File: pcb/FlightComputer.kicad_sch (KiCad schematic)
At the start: 74 parts, among them J1 USB4105-GF-A, Q1 DMG3415U, Q2 Si2319CDS, Q3 Si2319CDS, SW1 RESET, SW2 BOOT, U2 ICM-42670-P, U3 ESP32-C3-MINI-1, U5 SY8088, U6 MCP73831T-2ACI/OT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

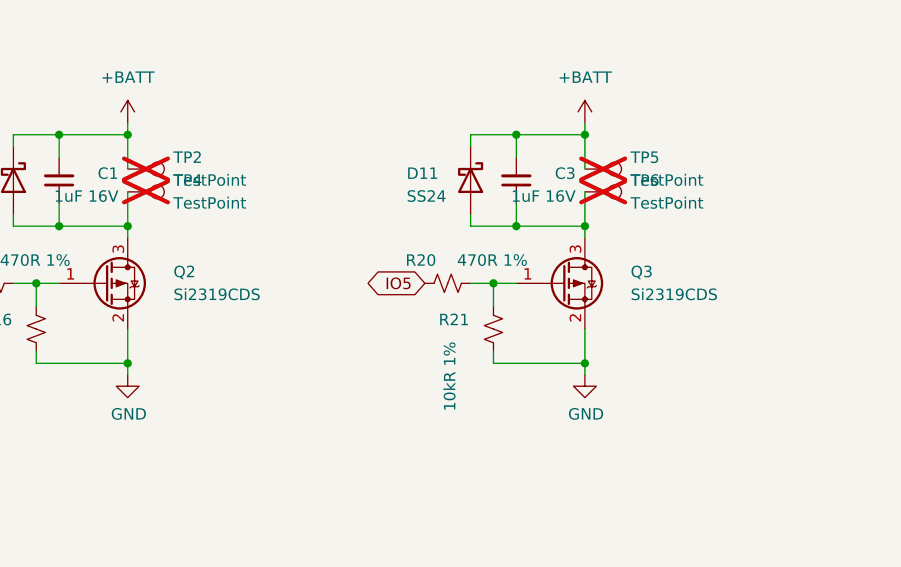
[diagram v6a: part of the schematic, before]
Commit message: change Si2319CDS to Si2302CDS
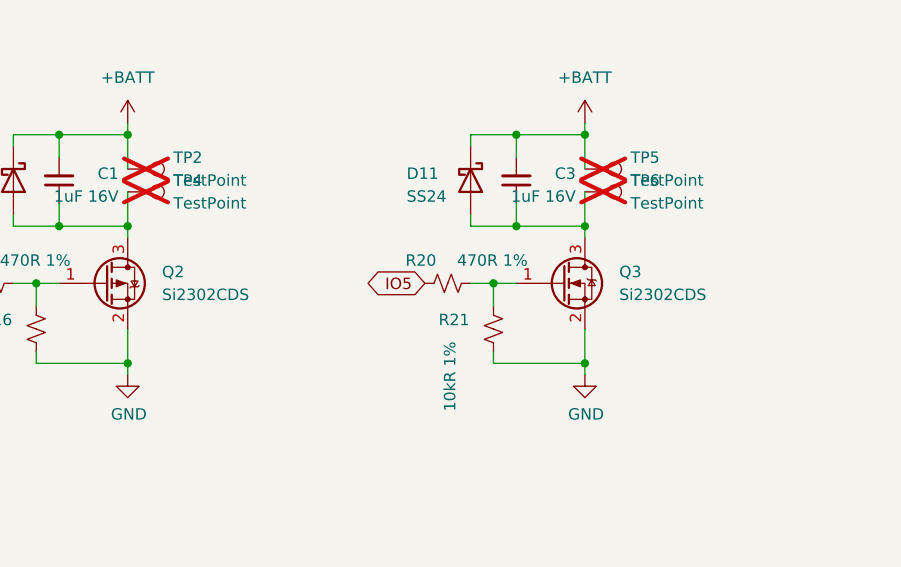
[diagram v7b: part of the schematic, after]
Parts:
- Q2: value Si2319CDS -> Si2302CDS; LCSC C146287 -> C10488
- Q3: value Si2319CDS -> Si2302CDS; symbol Transistor_FET:Si2319CDS -> Device:Q_NMOS_GSD; LCSC C146287 -> C10488
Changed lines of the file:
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@@
 		(fields_autoplaced yes)
 		(property "Reference" "Q2"
-			(at 185.42 246.3799 0)
-			(effects
-				(font
-					(size 1.27 1.27)
-				)
-				(justify left)
-			)
-		)
-		(property "Value" "Si2319CDS"
-			(at 185.42 248.9199 0)
+			(at 184.15 246.3799 0)
+			(effects
+				(font
+					(size 1.27 1.27)
+				)
+				(justify left)
+			)
+		)
+		(property "Value" "Si2302CDS"
+			(at 184.15 248.9199 0)
 			(effects
 				(font
@@
 			)
 		)
-		(property "LCSC" "C146287"
+		(property "LCSC" "C10488"
 			(at 177.8 247.65 0)
 			(effects
@@
 	)
 	(symbol
-		(lib_id "Transistor_FET:Si2319CDS")
+		(lib_id "Device:Q_NMOS_GSD")
 		(at 228.6 247.65 0)
 		(unit 1)
@@
 		(fields_autoplaced yes)
 		(property "Reference" "Q3"
-			(at 236.22 246.3799 0)
-			(effects
-				(font
-					(size 1.27 1.27)
-				)
-				(justify left)
-			)
-		)
-		(property "Value" "Si2319CDS"
-			(at 236.22 248.9199 0)
+			(at 234.95 246.3799 0)
+			(effects
+				(font
+					(size 1.27 1.27)
+				)
+				(justify left)
+			)
+		)
+		(property "Value" "Si2302CDS"
+			(at 234.95 248.9199 0)
 			(effects
 				(font
@@
 		)
 		(property "Footprint" "Package_TO_SOT_SMD:SOT-23"
-			(at 233.68 249.555 0)
-			(effects
-				(font
-					(size 1.27 1.27)
-					(italic yes)
-				)
-				(justify left)
-				(hide yes)
-			)
-		)
-		(property "Datasheet" "http://www.vishay.com/docs/66709/si2319cd.pdf"
-			(at 233.68 251.46 0)
-			(effects
-				(font
-					(size 1.27 1.27)
-				)
-				(justify left)
-				(hide yes)
-			)
-		)
-		(property "Description" "-4.4A Id, -40V Vds, P-Channel MOSFET, SOT-23"
+			(at 233.68 245.11 0)
+			(effects
+				(font
+					(size 1.27 1.27)
+				)
+				(hide yes)
+			)
+		)
+		(property "Datasheet" "~"
 			(at 228.6 247.65 0)
 			(effects
@@
 			)
 		)
-		(property "LCSC" "C146287"
+		(property "Description" "N-MOSFET transistor, gate/source/drain"
 			(at 228.6 247.65 0)
 			(effects
+				(font
+					(size 1.27 1.27)
+				)
+				(hide yes)
+			)
+		)
+		(property "LCSC" "C10488"
+			(at 228.6 247.65 0)
+			(effects

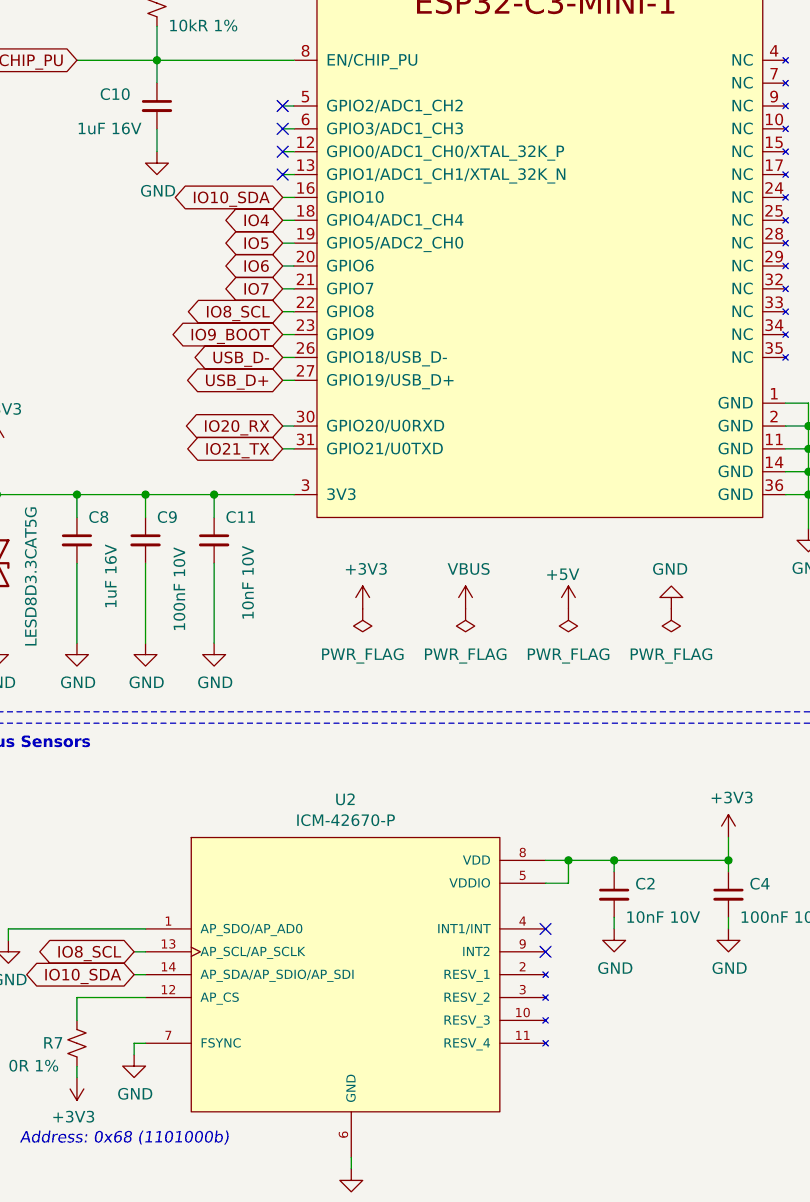
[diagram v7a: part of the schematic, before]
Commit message: Connect IO0 to IMU interrupt
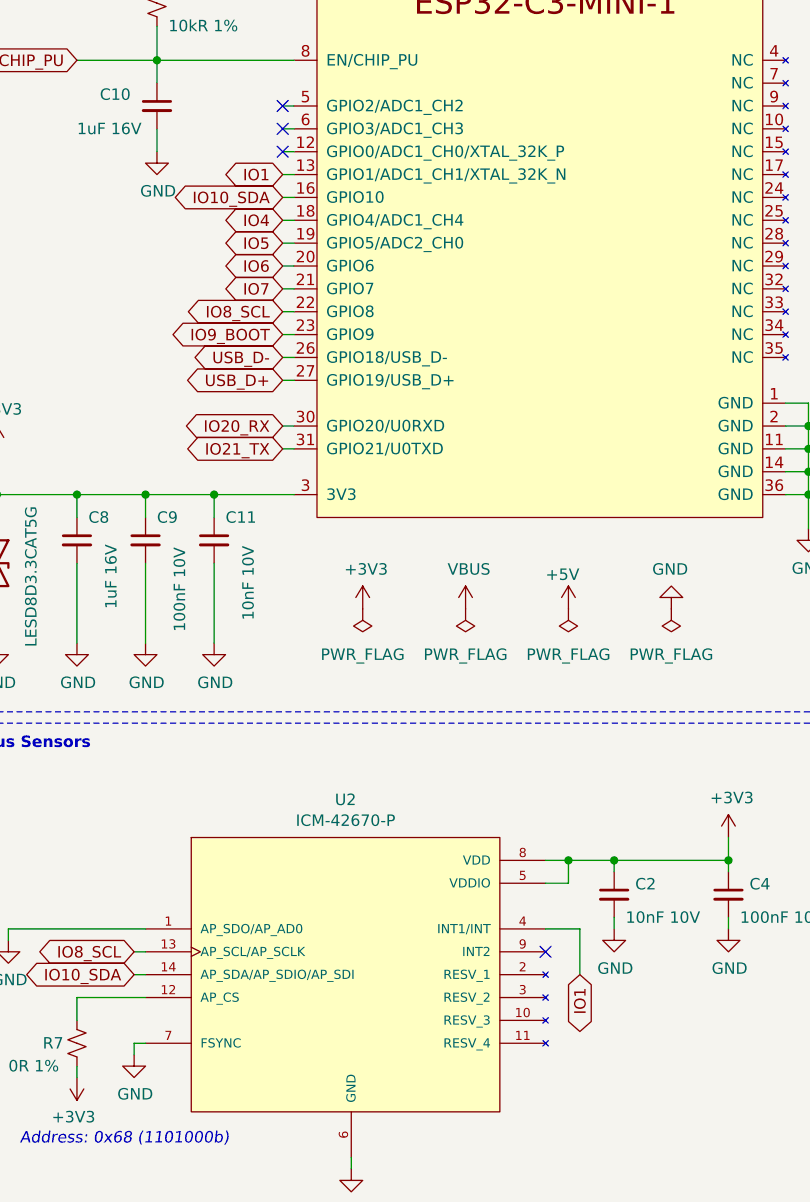
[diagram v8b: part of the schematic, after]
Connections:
- net IO1: now reaches U2.4 (INT1/INT)
- net IO1: now also U3.13 (GPIO1/ADC1_CH1/XTAL_32K_N)
- no-connect marks 10 -> 8
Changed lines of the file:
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@@
 	)
 	(no_connect
-		(at 80.01 134.62)
-	)
-	(no_connect
 		(at 214.63 153.67)
 	)
@@
 	)
 	(no_connect
-		(at 50.8 48.26)
+		(at 50.8 43.18)
 	)
 	(no_connect
@@
 	)
 	(no_connect
-		(at 50.8 43.18)
-	)
-	(no_connect
 		(at 71.12 261.62)
 	)
@@
 	)
 	(no_connect
-		(at 80.01 132.08)
+		(at 80.01 134.62)
 	)
 	(wire
@@
 	(wire
 		(pts
+			(xy 80.01 132.08) (xy 83.82 132.08)
+		)
+		(stroke
+			(width 0)
+			(type default)
+		)
+	)
+	(wire
+		(pts
 			(xy 256.54 36.83) (xy 256.54 38.1)
 		)
@@
 	(wire
 		(pts
+			(xy 83.82 132.08) (xy 83.82 137.16)
+		)
+		(stroke
+			(width 0)
+			(type default)
+		)
+	)
+	(wire
+		(pts
 			(xy 27.94 86.36) (xy 27.94 83.82)
 		)
@@
 		)
 	)
+	(global_label "IO1"
+		(shape bidirectional)
+		(at 50.8 48.26 180)
+		(fields_autoplaced yes)
+		(effects
+			(font
+				(size 1.27 1.27)
+			)
+			(justify right)
+		)
+		(property "Intersheetrefs" "${INTERSHEET_REFS}"
+			(at 44.3717 48.26 0)
+			(effects
+				(font
+					(size 1.27 1.27)
+				)
+				(justify right)
+				(hide yes)
+			)
+		)
+	)
 	(global_label "USB_D+"
 		(shape bidirectional)
@@
 			(effects
 				(font
+					(size 1.27 1.27)
+				)
+				(justify right)
+				(hide yes)
+			)
+		)
+	)
+	(global_label "IO1"
+		(shape bidirectional)
+		(at 83.82 137.16 270)
+		(fields_autoplaced yes)
+		(effects
+			(font
+				(size 1.27 1.27)
+			)
+			(justify right)
+		)
+		(property "Intersheetrefs" "${INTERSHEET_REFS}"
+			(at 83.82 143.5883 90)
+			(effects
+				(font
